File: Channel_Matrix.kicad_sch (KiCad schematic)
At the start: 16 parts, among them U2001 LP38690SDX-3.3/NOPB

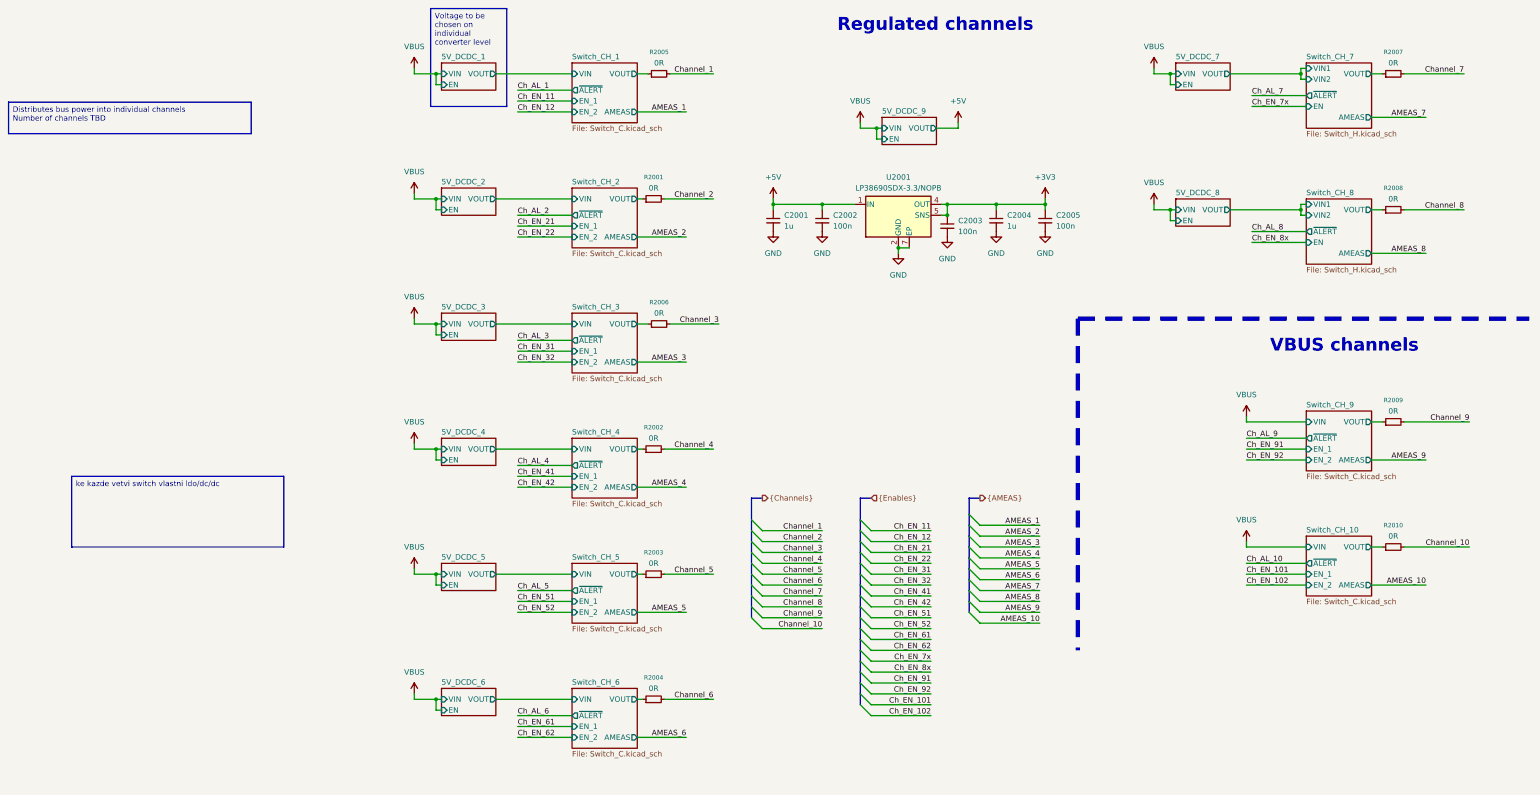
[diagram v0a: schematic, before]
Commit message: deleted unused sheets, added standalone current measure sheet
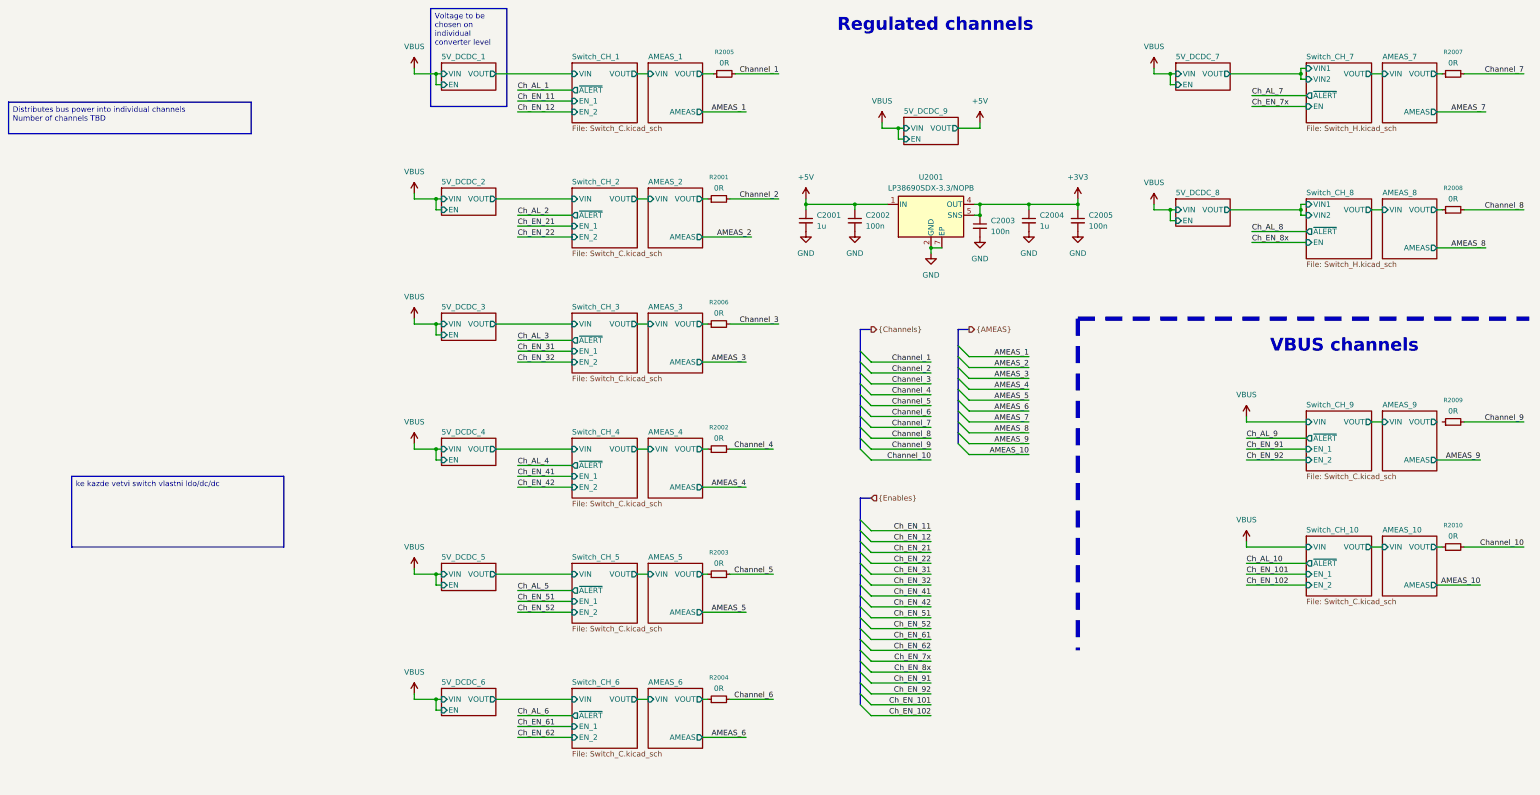
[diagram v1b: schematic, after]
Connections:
- net Switch_CH_1/VOUT renamed AMEAS_1/VOUT
- net Switch_CH_10/VOUT renamed AMEAS_10/VOUT
- net Switch_CH_2/VOUT renamed AMEAS_2/VOUT
- net Switch_CH_3/VOUT renamed AMEAS_3/VOUT
- net Switch_CH_4/VOUT renamed AMEAS_4/VOUT
- net Switch_CH_5/VOUT renamed AMEAS_5/VOUT
- net Switch_CH_6/VOUT renamed AMEAS_6/VOUT
- net Switch_CH_7/VOUT renamed AMEAS_7/VOUT
- net Switch_CH_8/VOUT renamed AMEAS_8/VOUT
- net Switch_CH_9/VOUT: no longer names the net of R2009.1
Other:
- added sheet AMEAS_1 (Current_Measure.kicad_sch)
- added sheet AMEAS_10 (Current_Measure.kicad_sch)
- added sheet AMEAS_2 (Current_Measure.kicad_sch)
- added sheet AMEAS_3 (Current_Measure.kicad_sch)
- added sheet AMEAS_4 (Current_Measure.kicad_sch)
- added sheet AMEAS_5 (Current_Measure.kicad_sch)
- added sheet AMEAS_6 (Current_Measure.kicad_sch)
- added sheet AMEAS_7 (Current_Measure.kicad_sch)
- added sheet AMEAS_8 (Current_Measure.kicad_sch)
- added sheet AMEAS_9 (Current_Measure.kicad_sch)
- sheet 5V_DCDC_1: file LDO_5V.kicad_sch -> DCDC_ADJUCTABLE.kicad_sch
- sheet 5V_DCDC_2: file LDO_5V.kicad_sch -> DCDC_ADJUCTABLE.kicad_sch
- sheet 5V_DCDC_3: file LDO_5V.kicad_sch -> DCDC_ADJUCTABLE.kicad_sch
- sheet 5V_DCDC_4: file LDO_5V.kicad_sch -> DCDC_ADJUCTABLE.kicad_sch
- sheet 5V_DCDC_5: file LDO_5V.kicad_sch -> DCDC_ADJUCTABLE.kicad_sch
- sheet 5V_DCDC_6: file LDO_5V.kicad_sch -> DCDC_ADJUCTABLE.kicad_sch
- sheet 5V_DCDC_7: file LDO_5V.kicad_sch -> DCDC_ADJUCTABLE.kicad_sch
- sheet 5V_DCDC_8: file LDO_5V.kicad_sch -> DCDC_ADJUCTABLE.kicad_sch
- sheet Switch_CH_1 ports: added none; removed AMEAS
- sheet Switch_CH_10 ports: added none; removed AMEAS
- sheet Switch_CH_2 ports: added none; removed AMEAS
- sheet Switch_CH_3 ports: added none; removed AMEAS
- sheet Switch_CH_4 ports: added none; removed AMEAS
- sheet Switch_CH_5 ports: added none; removed AMEAS
- sheet Switch_CH_6 ports: added none; removed AMEAS
- sheet Switch_CH_7 ports: added none; removed AMEAS
- sheet Switch_CH_8 ports: added none; removed AMEAS
- sheet Switch_CH_9 ports: added none; removed AMEAS
- moved on the sheet: C2001, C2002, C2003, C2004, C2005, R2001, R2002, R2003, R2004, R2005, R2006, R2007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

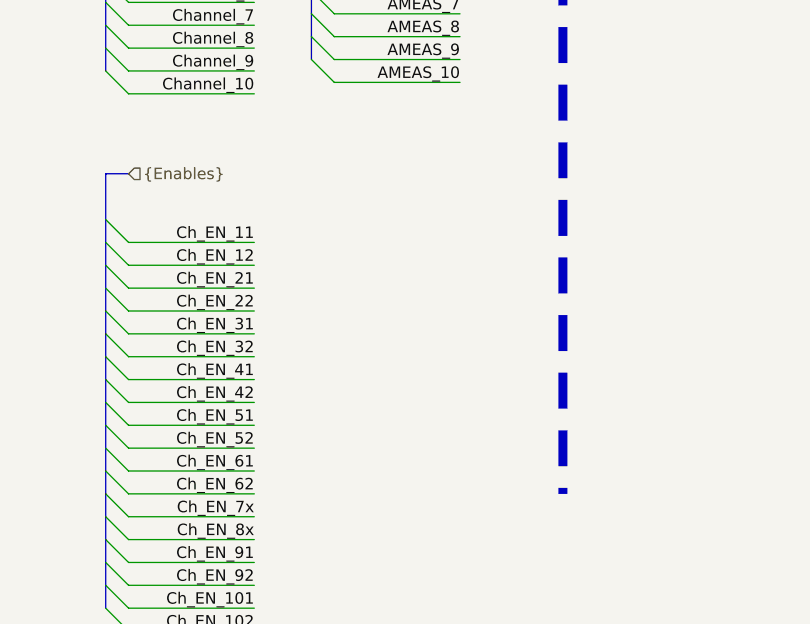
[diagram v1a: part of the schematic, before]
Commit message: wired channel alerts; added schematic for test pbc
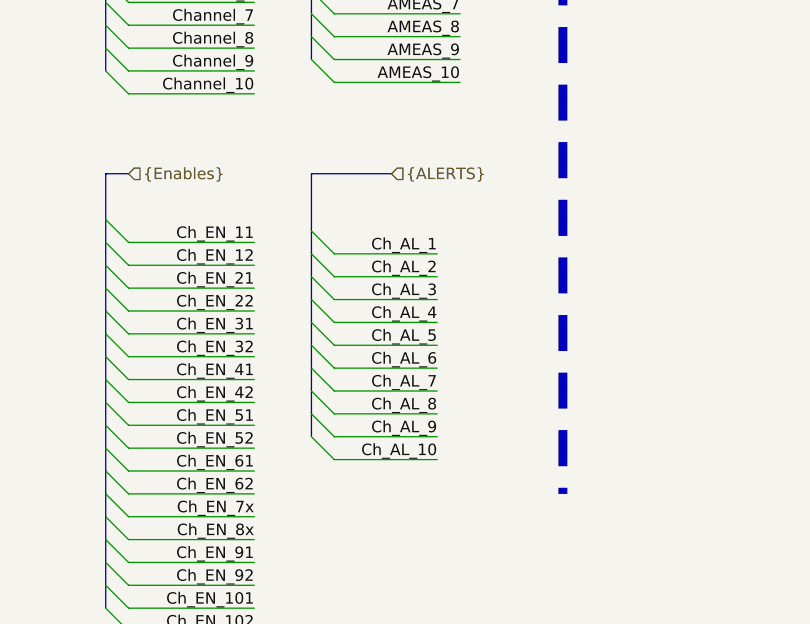
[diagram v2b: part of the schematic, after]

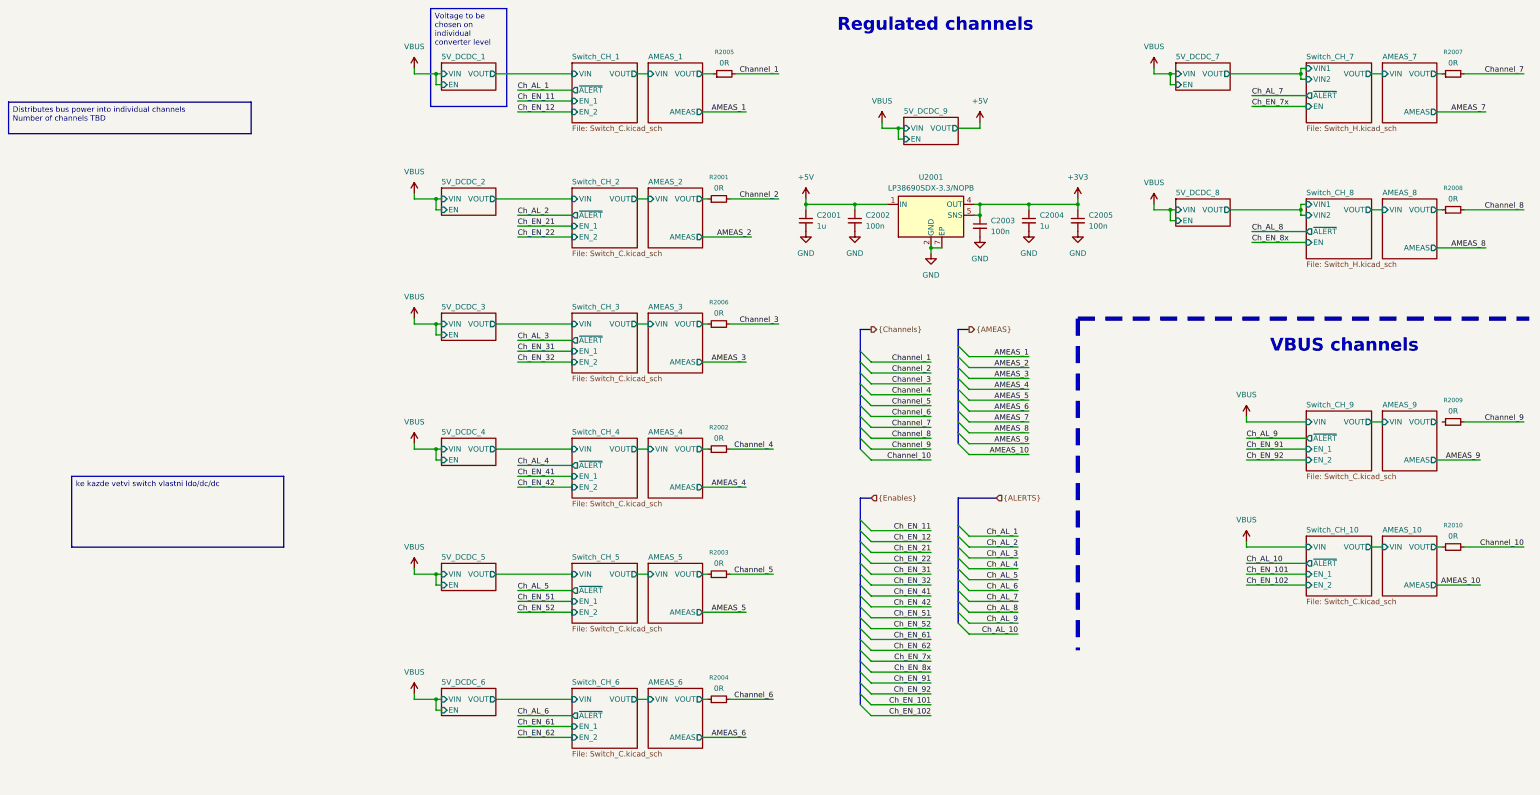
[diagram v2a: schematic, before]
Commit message: reduced number of DCDC converter for PV panels; updated test pcb
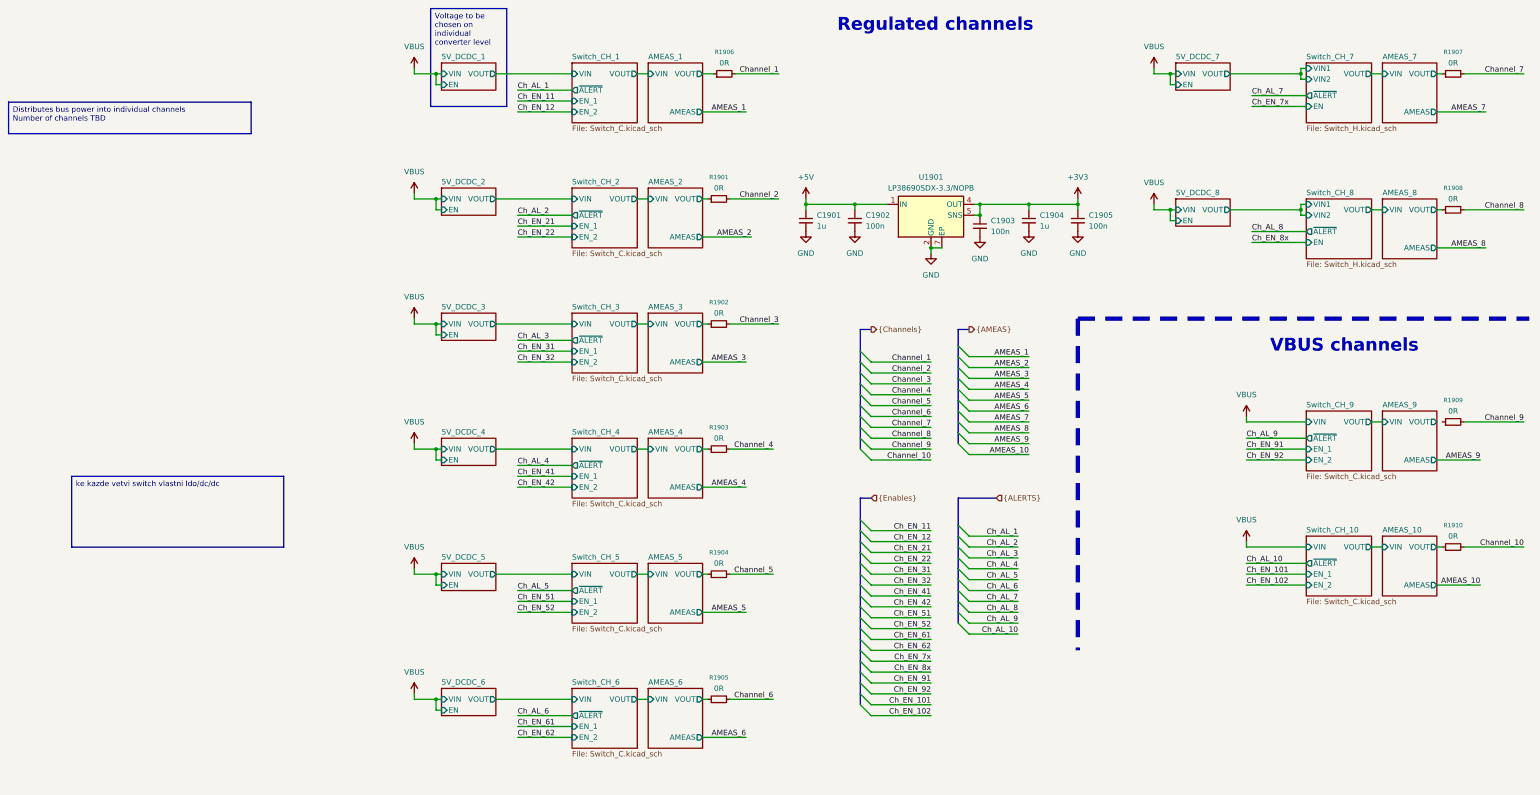
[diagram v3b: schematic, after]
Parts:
- renumbered C2001 to C1901, C2002 to C1902, C2003 to C1903, C2004 to C1904, C2005 to C1905, R2001 to R1901, R2006 to R1902, R2002 to R1903, R2003 to R1904, R2004 to R1905, R2005 to R1906, R2007 to R1907, R2008 to R1908, R2009 to R1909, R2010 to R1910, U2001 to U1901
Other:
- removed sheet 5V_DCDC_9

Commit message: added missing heater connectors
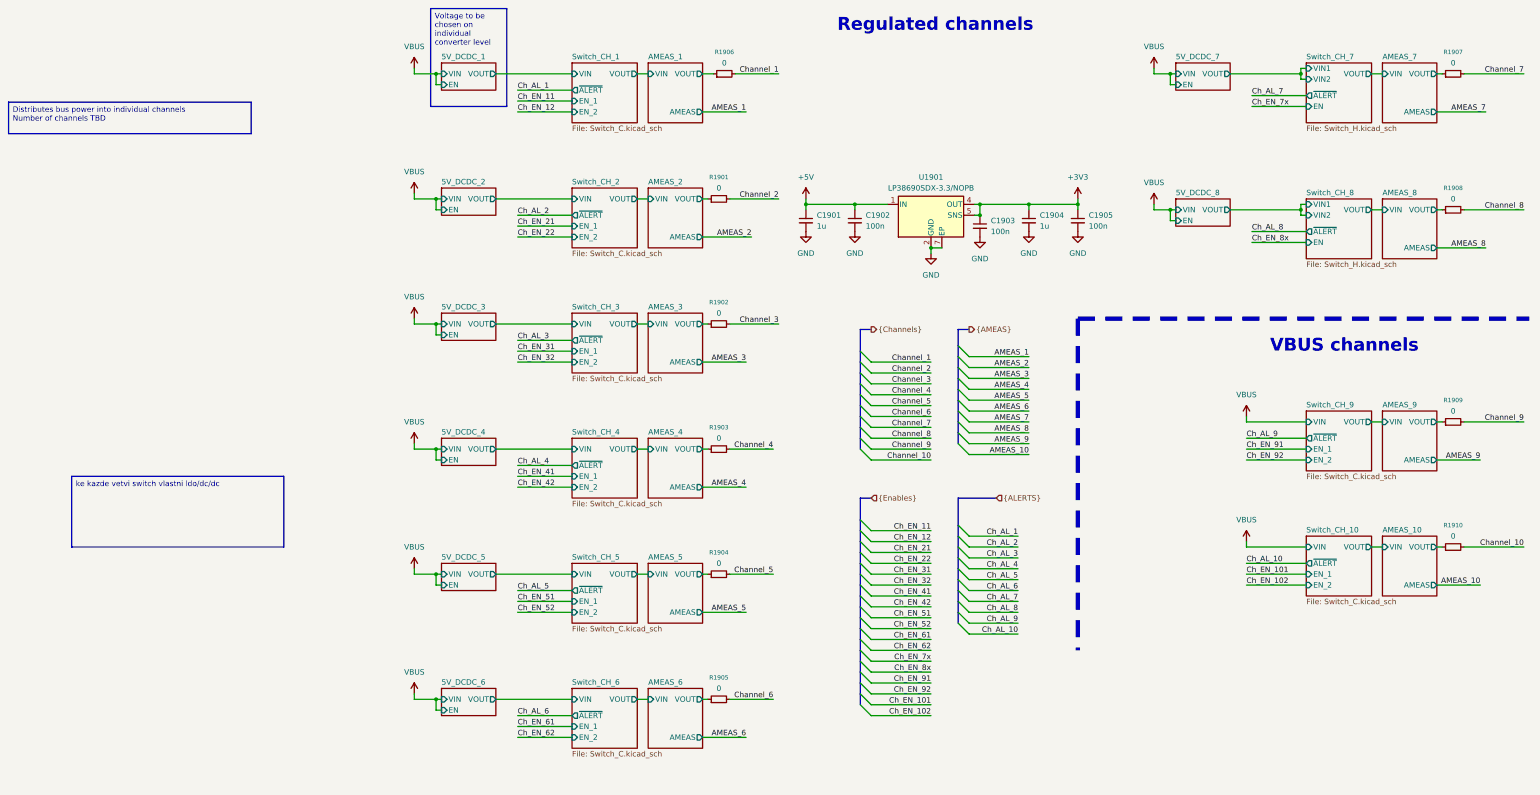
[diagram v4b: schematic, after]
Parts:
- R1901, R1902, R1903, R1904, R1905, R1906, R1907, R1908, R1909, R1910: value 0R -> 0
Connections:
- net AMEAS_9/VOUT: now also R1909.1
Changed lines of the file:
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@@
 	(wire
 		(pts
+			(xy 260.35 111.76) (xy 261.62 111.76)
+		)
+		(stroke
+			(width 0)
+			(type default)
+		)
+	)
+	(wire
+		(pts
 			(xy 88.9 88.9) (xy 90.17 88.9)
 		)
@@
 			)
 		)
-		(property "Value" "0R"
+		(property "Value" "0"
 			(at 92.71 173.99 90)
 			(effects
@@
 			)
 		)
-		(property "Value" "0R"
+		(property "Value" "0"
 			(at 92.71 144.78 90)
 			(effects
@@
 			)
 		)
-		(property "Value" "0R"
+		(property "Value" "0"
 			(at 264.16 109.22 90)
 			(effects
@@
 			)
 		)
-		(property "Value" "0R"
+		(property "Value" "0"
 			(at 92.71 86.36 90)
 			(effects
@@
 			)
 		)
-		(property "Value" "0R"
+		(property "Value" "0"
 			(at 264.16 59.69 90)
 			(effects
@@
 			)
 		)
-		(property "Value" "0R"
+		(property "Value" "0"
 			(at 264.16 138.43 90)
 			(effects
@@
 			)
 		)
-		(property "Value" "0R"
+		(property "Value" "0"
 			(at 93.98 27.94 90)
 			(effects
@@
 			)
 		)
-		(property "Value" "0R"
+		(property "Value" "0"
 			(at 92.71 115.57 90)
 			(effects
@@
 			)
 		)
-		(property "Value" "0R"
+		(property "Value" "0"
 			(at 264.16 27.94 90)
 			(effects
@@
 			)
 		)
-		(property "Value" "0R"
+		(property "Value" "0"
 			(at 92.71 57.15 90)
 			(effects

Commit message: restructurization of the entire project improved
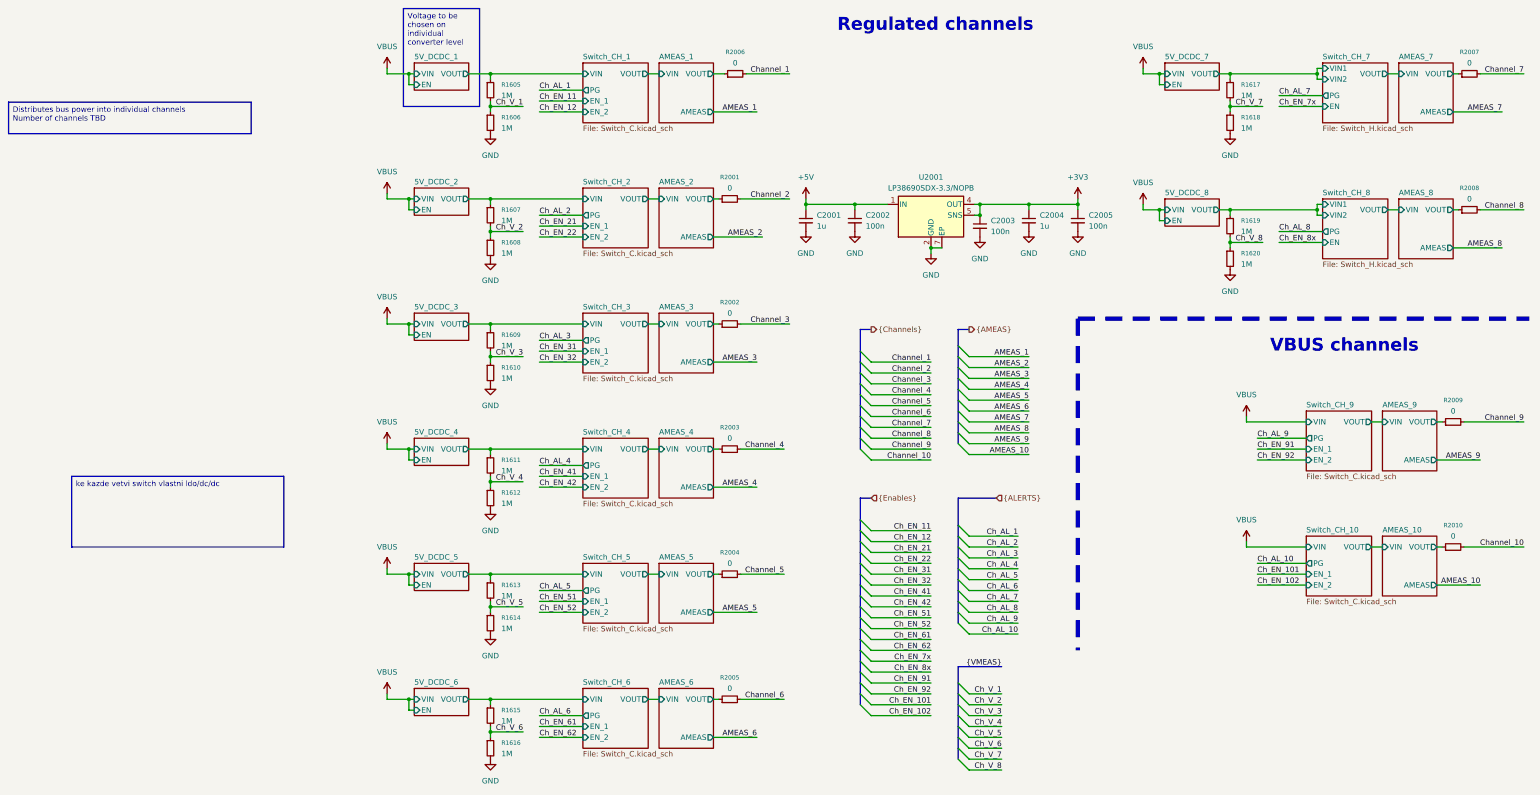
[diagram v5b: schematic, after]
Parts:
- added R1605, R1606, R1607, R1608, R1609, R1610, R1611, R1612, R1613, R1614, R1615, R1616, R1617, R1618, R1619, R1620: 1M, Resistor_SMD:R_0603_1608Metric_Pad0.98x0.95mm_HandSolder, symbol Device:R_Small
- renumbered C1901 to C2001, C1902 to C2002, C1903 to C2003, C1904 to C2004, C1905 to C2005, R1901 to R2001, R1902 to R2002, R1903 to R2003, R1904 to R2004, R1905 to R2005, R1906 to R2006, R1907 to R2007, R1908 to R2008, R1909 to R2009, R1910 to R2010, U1901 to U2001
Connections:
- net 5V_DCDC_1/VOUT: now also R1605.1
- net 5V_DCDC_2/VOUT: now also R1607.1
- net 5V_DCDC_3/VOUT: now also R1609.1
- net 5V_DCDC_4/VOUT: now also R1611.1
- net 5V_DCDC_5/VOUT: now also R1613.1
- net 5V_DCDC_6/VOUT: now also R1615.1
- net 5V_DCDC_7/VOUT: now also R1617.1
- net 5V_DCDC_8/VOUT: now also R1619.1
- net GND: now also R1606.2, R1608.2, R1610.2, R1612.2, R1614.2, R1616.2, R1618.2, R1620.2
- new net Ch_V_1: R1605.2, R1606.1
- new net Ch_V_2: R1607.2, R1608.1
- new net Ch_V_3: R1609.2, R1610.1
- new net Ch_V_4: R1611.2, R1612.1
- new net Ch_V_5: R1613.2, R1614.1
- new net Ch_V_6: R1615.2, R1616.1
- new net Ch_V_7: R1617.2, R1618.1
- new net Ch_V_8: R1619.2, R1620.1
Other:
- sheet Switch_CH_1 ports: added PG; removed ~{ALERT}
- sheet Switch_CH_10 ports: added PG; removed ~{ALERT}
- sheet Switch_CH_2 ports: added PG; removed ~{ALERT}
- sheet Switch_CH_3 ports: added PG; removed ~{ALERT}
- sheet Switch_CH_4 ports: added PG; removed ~{ALERT}
- sheet Switch_CH_5 ports: added PG; removed ~{ALERT}
- sheet Switch_CH_6 ports: added PG; removed ~{ALERT}
- sheet Switch_CH_7 ports: added PG; removed ~{ALERT}
- sheet Switch_CH_8 ports: added PG; removed ~{ALERT}
- sheet Switch_CH_9 ports: added PG; removed ~{ALERT}
- moved on the sheet: R2001, R2002, R2003, R2004, R2005, R2006, R2007, R2008
